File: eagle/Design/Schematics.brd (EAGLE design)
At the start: 101.6 x 55.9 mm, 66 parts, among them IC1 LM1117, IC2 CY7C68013A-56PVXC, IC3 ADS7042DCU, IC4 ADS7042DCU, Q1 SI2369DS, Q2 24MHz, X1 MPT2, X10 MPT3, X11 MPT2, X12 MPT2, X13 MPT2, X14 MPT2, X15 MPT2, X16 MPT2, X2 PN61729-S, X3 MPT2, X4 MPT2, X5 MPT2, X6 MPT2, X7 MPT2, X8 MPT2, X9 MPT3

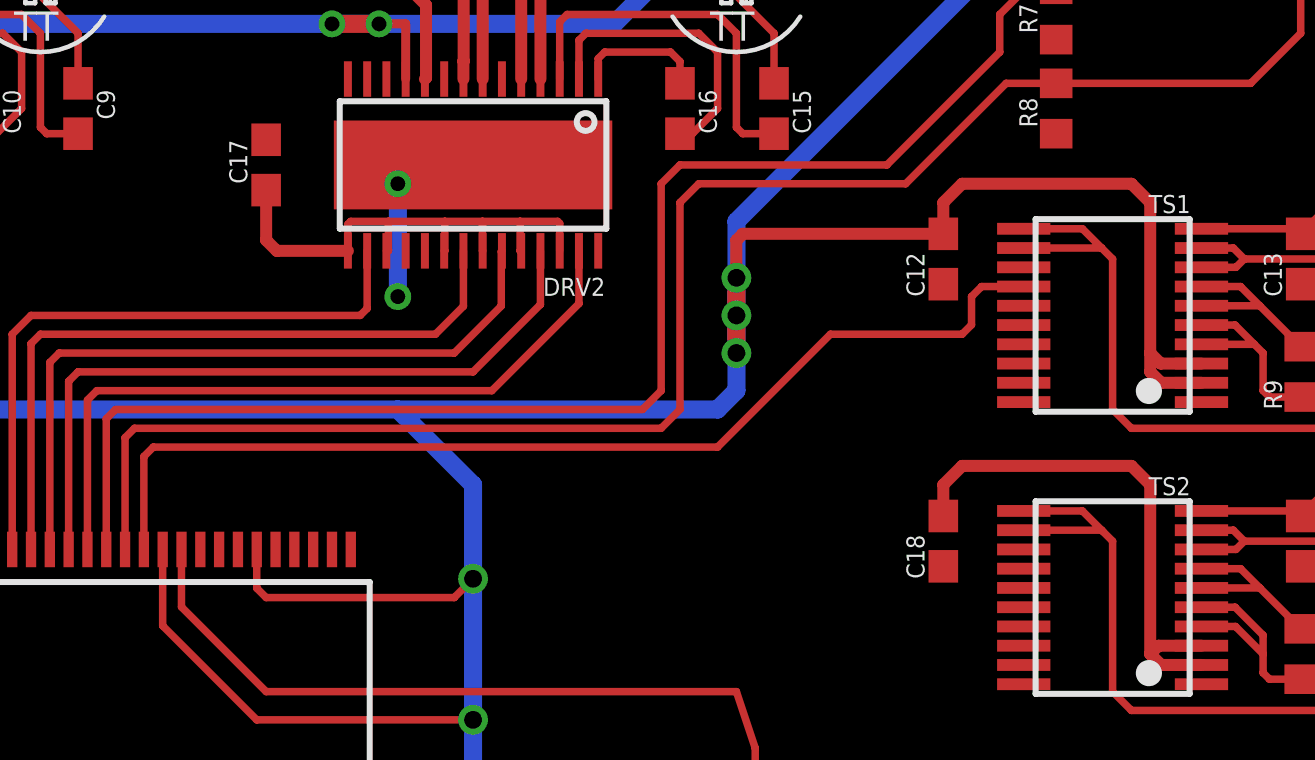
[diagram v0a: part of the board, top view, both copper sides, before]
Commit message: Routed nets for Temp Sensor #1.
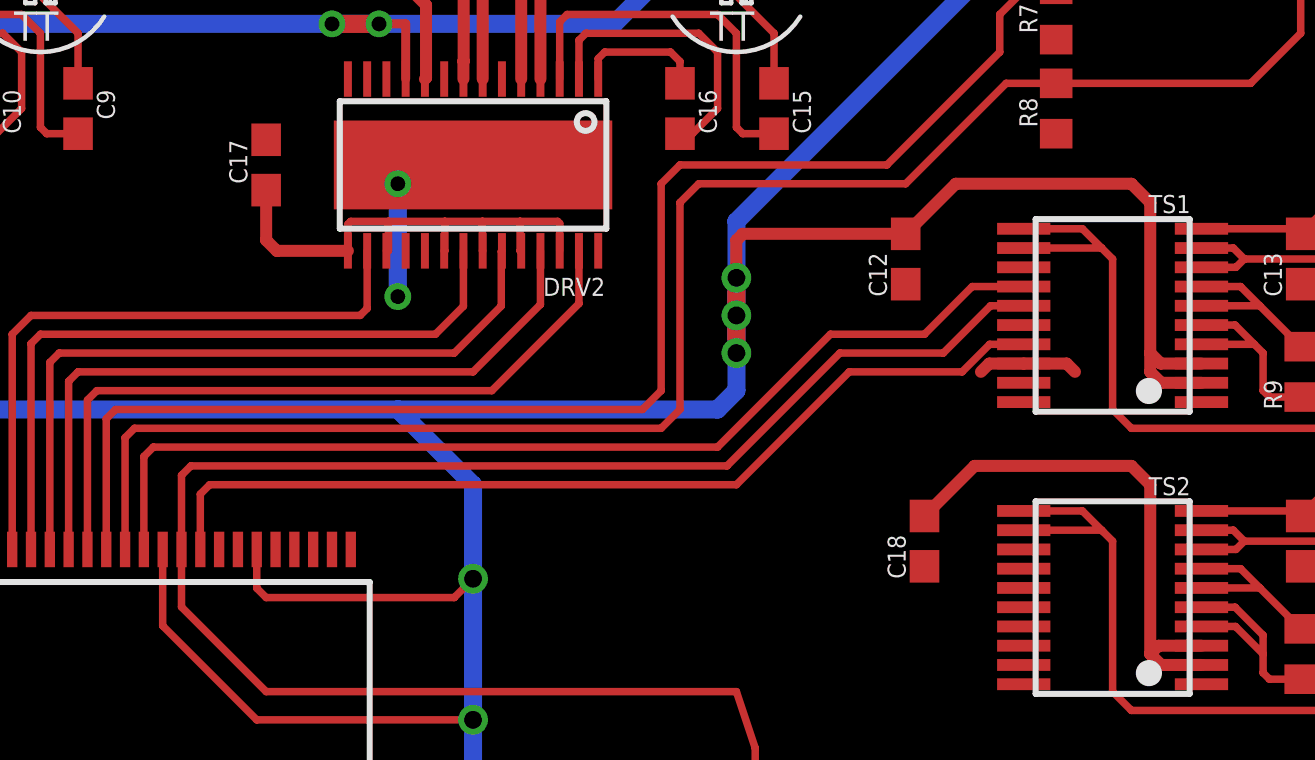
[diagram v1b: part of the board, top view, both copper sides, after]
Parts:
- moved C12 1.27 mm to (75.6, 34.9)
- moved C18 0.63 mm to (76.2, 25.4)
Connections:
- net SPI_SDO: now also IC2.37; no longer IC2.36
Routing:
- net SPI_SCLK: track 27.7 -> 61.0 mm
- net SPI_SDO: track 0.00 -> 31.8 mm
- net GND: track 8.89 -> 12.3 mm
- net +3P3V: track 358.5 -> 357.9 mm
- net SPI_SDI: track 35.8 -> 35.2 mm
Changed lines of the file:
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@@
 <attribute name="NAME" x="95.758" y="27.559" size="0.6096" layer="25" rot="R270"/>
 </element>
-<element name="C12" library="resistor" package="C0603" value="200n" x="76.835" y="34.925" smashed="yes" rot="R270">
-<attribute name="NAME" x="76.2" y="33.655" size="0.6096" layer="25" rot="R90"/>
-</element>
-<element name="C18" library="resistor" package="C0603" value="200n" x="76.835" y="25.4" smashed="yes" rot="R270">
-<attribute name="NAME" x="76.2" y="24.13" size="0.6096" layer="25" rot="R90"/>
+<element name="C12" library="resistor" package="C0603" value="200n" x="75.565" y="34.925" smashed="yes" rot="R270">
+<attribute name="NAME" x="74.93" y="33.655" size="0.6096" layer="25" rot="R90"/>
+</element>
+<element name="C18" library="resistor" package="C0603" value="200n" x="76.2" y="25.4" smashed="yes" rot="R270">
+<attribute name="NAME" x="75.565" y="24.13" size="0.6096" layer="25" rot="R90"/>
 </element>
 <element name="C13" library="resistor" package="C0603" value="100n" x="88.9" y="34.925" smashed="yes" rot="R270">
@@
 <contactref element="C12" pad="2"/>
 <contactref element="C18" pad="2"/>
-<wire x1="79.55" y1="25.12" x2="79.55" y2="21.87" width="0" layer="19" extent="1-1"/>
-<wire x1="79.55" y1="31.395" x2="79.55" y2="34.645" width="0" layer="19" extent="1-1"/>
+<wire x1="79.55" y1="31.395" x2="78.385" y2="31.395" width="0.4064" layer="1"/>
+<wire x1="78.385" y1="31.395" x2="78.105" y2="31.115" width="0.4064" layer="1"/>
+<wire x1="79.55" y1="31.395" x2="81" y2="31.395" width="0.4064" layer="1"/>
+<wire x1="81" y1="31.395" x2="81.28" y2="31.115" width="0.4064" layer="1"/>
+<wire x1="79.55" y1="21.87" x2="79.55" y2="25.12" width="0" layer="19" extent="1-1"/>
 </signal>
 <signal name="+3P3V">
@@
 <wire x1="83.82" y1="31.75" x2="83.82" y2="36.83" width="0.4064" layer="1"/>
 <wire x1="83.82" y1="36.83" x2="83.185" y2="37.465" width="0.4064" layer="1"/>
-<wire x1="83.185" y1="37.465" x2="77.47" y2="37.465" width="0.4064" layer="1"/>
-<wire x1="77.47" y1="37.465" x2="76.835" y2="36.83" width="0.4064" layer="1"/>
-<wire x1="76.835" y1="36.83" x2="76.835" y2="35.775" width="0.4064" layer="1"/>
 <wire x1="85.55" y1="30.745" x2="84.19" y2="30.745" width="0.4064" layer="1"/>
 <wire x1="84.19" y1="30.745" x2="83.82" y2="31.115" width="0.4064" layer="1"/>
 <wire x1="83.82" y1="31.115" x2="83.82" y2="31.75" width="0.4064" layer="1"/>
-<wire x1="76.835" y1="26.25" x2="76.835" y2="27.305" width="0.4064" layer="1"/>
-<wire x1="76.835" y1="27.305" x2="77.47" y2="27.94" width="0.4064" layer="1"/>
-<wire x1="77.47" y1="27.94" x2="83.185" y2="27.94" width="0.4064" layer="1"/>
 <wire x1="83.185" y1="27.94" x2="83.82" y2="27.305" width="0.4064" layer="1"/>
 <wire x1="83.82" y1="27.305" x2="83.82" y2="21.59" width="0.4064" layer="1"/>
@@
 <wire x1="85.55" y1="21.87" x2="84.1" y2="21.87" width="0.4064" layer="1"/>
 <wire x1="84.1" y1="21.87" x2="83.82" y2="21.59" width="0.4064" layer="1"/>
-<wire x1="76.835" y1="35.775" x2="70.065" y2="35.775" width="0.4064" layer="1"/>
+<wire x1="75.565" y1="35.775" x2="70.065" y2="35.775" width="0.4064" layer="1"/>
 <wire x1="70.065" y1="35.775" x2="69.85" y2="35.56" width="0.4064" layer="1"/>
 <wire x1="69.85" y1="35.56" x2="69.85" y2="34.29" width="0.4064" layer="1"/>
+<wire x1="83.185" y1="37.465" x2="77.255" y2="37.465" width="0.4064" layer="1"/>
+<wire x1="83.185" y1="27.94" x2="77.89" y2="27.94" width="0.4064" layer="1"/>
+<wire x1="77.89" y1="27.94" x2="76.2" y2="26.25" width="0.4064" layer="1"/>
+<wire x1="77.255" y1="37.465" x2="75.565" y2="35.775" width="0.4064" layer="1"/>
 <wire x1="84.19" y1="30.745" x2="83.185" y2="27.94" width="0" layer="19" extent="1-1"/>
 </signal>
@@
 <wire x1="49.8475" y1="25.12" x2="49.8475" y2="28.2575" width="0.254" layer="1"/>
 <wire x1="49.8475" y1="28.2575" x2="50.165" y2="28.575" width="0.254" layer="1"/>
-<wire x1="79.55" y1="33.995" x2="78.1275" y2="33.995" width="0.254" layer="1"/>
-<wire x1="78.1275" y1="33.995" x2="77.7875" y2="33.655" width="0.254" layer="1"/>
-<wire x1="77.7875" y1="33.655" x2="77.7875" y2="32.7025" width="0.254" layer="1"/>
-<wire x1="77.7875" y1="32.7025" x2="77.47" y2="32.385" width="0.254" layer="1"/>
-<wire x1="77.47" y1="32.385" x2="73.025" y2="32.385" width="0.254" layer="1"/>
+<wire x1="79.55" y1="33.995" x2="77.81" y2="33.995" width="0.254" layer="1"/>
 <wire x1="73.025" y1="32.385" x2="69.215" y2="28.575" width="0.254" layer="1"/>
 <wire x1="69.215" y1="28.575" x2="50.165" y2="28.575" width="0.254" layer="1"/>
-<wire x1="77.47" y1="32.385" x2="79.55" y2="24.47" width="0" layer="19" extent="1-1"/>
+<wire x1="77.81" y1="33.995" x2="76.2" y2="32.385" width="0.254" layer="1"/>
+<wire x1="76.2" y1="32.385" x2="73.025" y2="32.385" width="0.254" layer="1"/>
+<wire x1="76.2" y1="32.385" x2="79.55" y2="24.47" width="0" layer="19" extent="1-1"/>
 </signal>
 <signal name="SPI_SDO">
 <contactref element="IC3" pad="3"/>
 <contactref element="IC4" pad="3"/>
-<contactref element="IC2" pad="36"/>
 <contactref element="TS2" pad="17"/>
 <contactref element="TS1" pad="17"/>
-<wire x1="79.55" y1="22.52" x2="79.55" y2="32.045" width="0" layer="19" extent="1-1"/>
+<contactref element="IC2" pad="37"/>
+<wire x1="51.7525" y1="25.12" x2="51.7525" y2="26.9875" width="0.254" layer="1"/>
+<wire x1="51.7525" y1="26.9875" x2="52.07" y2="27.305" width="0.254" layer="1"/>
+<wire x1="52.07" y1="27.305" x2="69.85" y2="27.305" width="0.254" layer="1"/>
+<wire x1="77.47" y1="31.115" x2="73.66" y2="31.115" width="0.254" layer="1"/>
+<wire x1="79.55" y1="32.045" x2="78.4" y2="32.045" width="0.254" layer="1"/>
+<wire x1="78.4" y1="32.045" x2="77.47" y2="31.115" width="0.254" layer="1"/>
+<wire x1="73.66" y1="31.115" x2="69.85" y2="27.305" width="0.254" layer="1"/>
+<wire x1="77.47" y1="31.115" x2="79.55" y2="22.52" width="0" layer="19" extent="1-1"/>
 <wire x1="77.19" y1="11.815" x2="79.55" y2="22.52" width="0" layer="19" extent="1-1"/>
 <wire x1="77.19" y1="4.195" x2="77.19" y2="11.815" width="0" layer="19" extent="1-1"/>
-<wire x1="52.3875" y1="25.12" x2="79.55" y2="22.52" width="0" layer="19" extent="1-1"/>
 </signal>
 <signal name="N$39">
@@
 <contactref element="TS2" pad="15"/>
 <contactref element="TS1" pad="15"/>
-<wire x1="79.55" y1="23.82" x2="79.55" y2="33.345" width="0" layer="19" extent="1-1"/>
-<wire x1="69.85" y1="20.32" x2="79.55" y2="23.82" width="0" layer="19" extent="1-1"/>
+<wire x1="51.1175" y1="25.12" x2="51.1175" y2="27.6225" width="0.254" layer="1"/>
+<wire x1="51.1175" y1="27.6225" x2="51.435" y2="27.94" width="0.254" layer="1"/>
+<wire x1="51.435" y1="27.94" x2="69.5325" y2="27.94" width="0.254" layer="1"/>
+<wire x1="79.55" y1="33.345" x2="78.43" y2="33.345" width="0.254" layer="1"/>
+<wire x1="78.43" y1="33.345" x2="76.835" y2="31.75" width="0.254" layer="1"/>
+<wire x1="76.835" y1="31.75" x2="73.3425" y2="31.75" width="0.254" layer="1"/>
+<wire x1="73.3425" y1="31.75" x2="69.5325" y2="27.94" width="0.254" layer="1"/>
+<wire x1="76.835" y1="31.75" x2="79.55" y2="23.82" width="0" layer="19" extent="1-1"/>
 <wire x1="70.485" y1="10.16" x2="70.485" y2="14.605" width="0" layer="19" extent="1-1"/>
 <wire x1="77.19" y1="12.315" x2="70.485" y2="10.16" width="0" layer="19" extent="1-1"/>

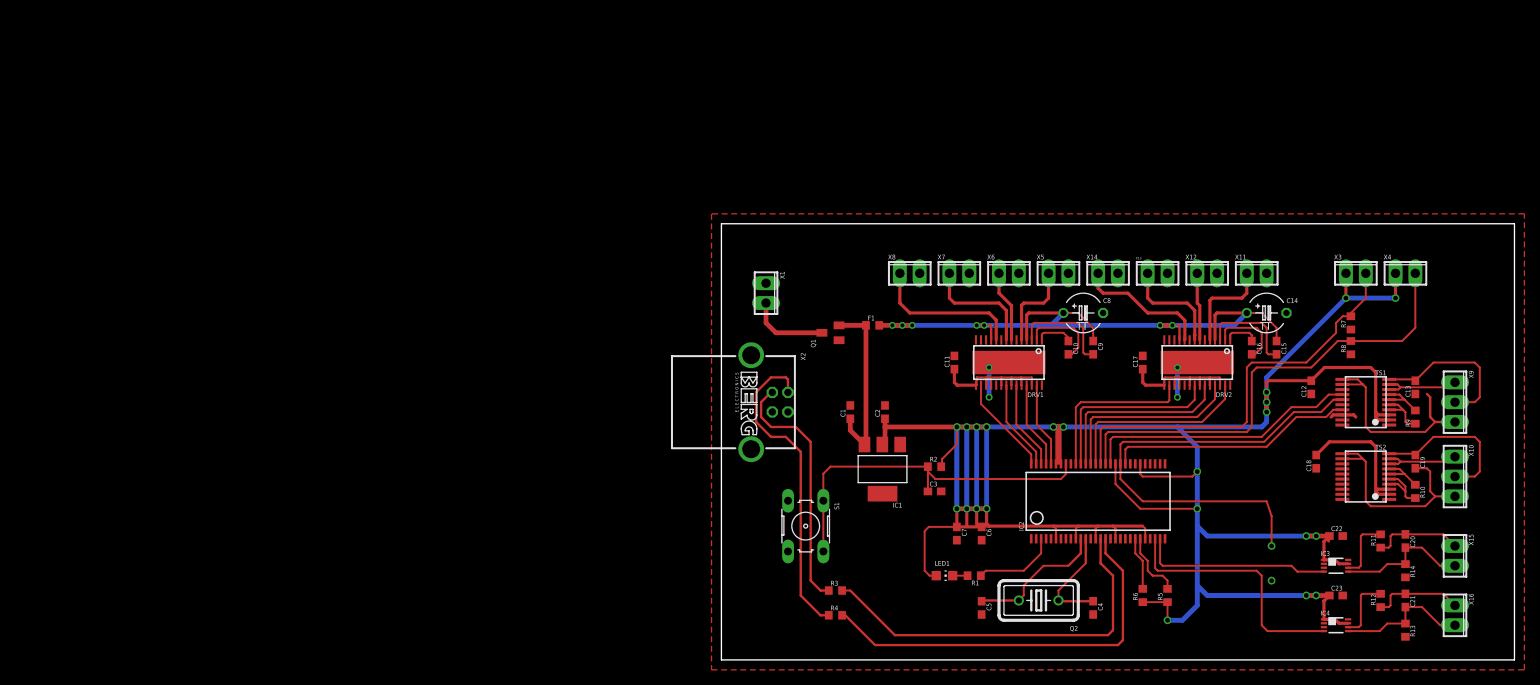
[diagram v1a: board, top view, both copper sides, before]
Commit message: Goodbye USB, hello Pi
Completely changed the direction of the hardware development.
Originally wanted to utilize a USB interface to plug into any PC but
found it was easier (and cheaper) to by a Raspberry Pi for $35 and build
an expansion board to control the brew hardware.  Created a barebone set
of schematics and layout.
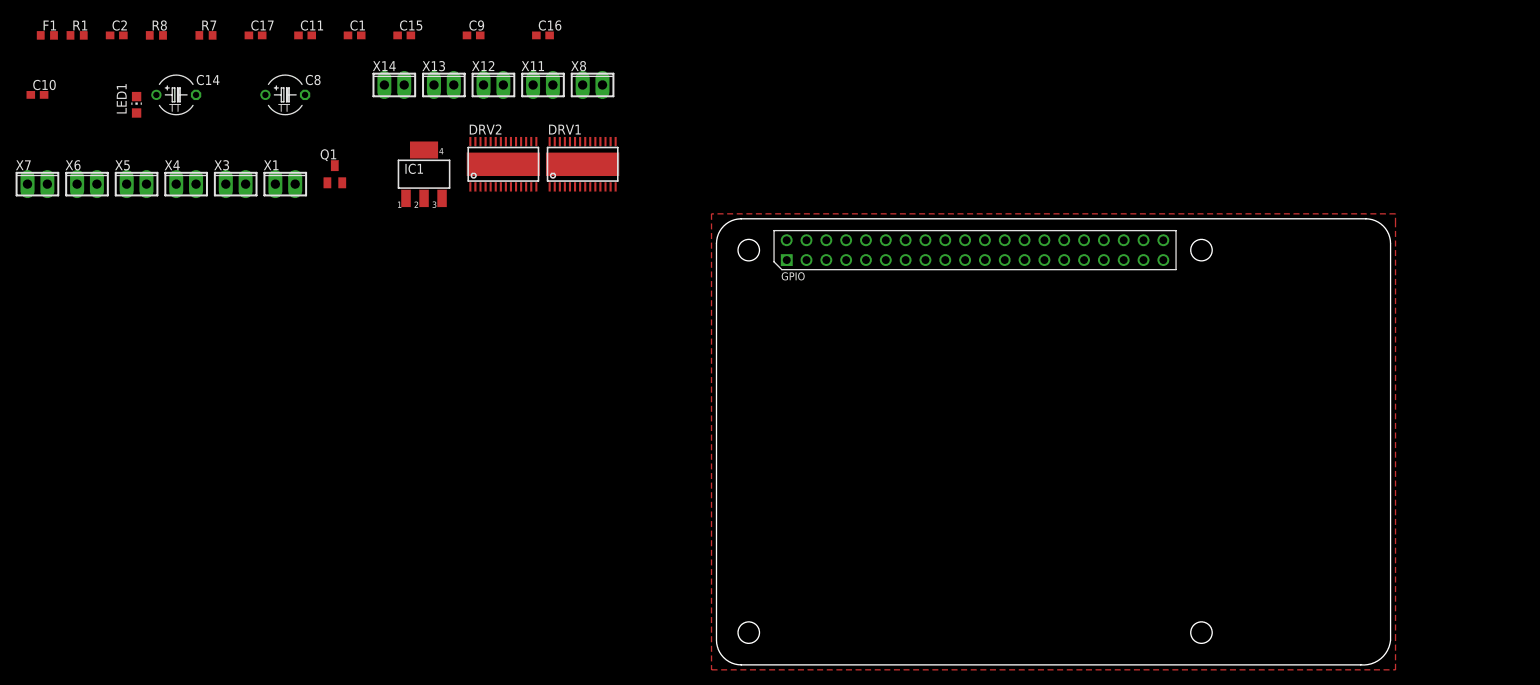
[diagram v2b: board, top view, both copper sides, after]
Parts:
- removed C12, C18: 200n, resistor:C0603
- removed C13, C19, C20, C21: 100n, resistor:C0603
- removed C22, C23: 1u, resistor:C0603
- removed C3, C7: .1u, resistor:C0603
- removed C4, C5: 27p, resistor:C0603
- removed C6: 2.2u, resistor:C0603
- removed IC2: CY7C68013A-56PVXC, cypress:SSOP56
- removed IC3, IC4: ADS7042DCU, texas:DCU_(R-PDSO-G8)
- removed Q2: 24MHz, crystal:HC18U-V
- removed R10, R9: 390 .1%, resistor:R0603
- removed R11, R12, R2: 100K, resistor:R0603
- removed R13, R14: DNS, resistor:R0603
- removed R3, R4: 22, resistor:R0603
- removed R5, R6: 2.2K, resistor:R0603
- removed S1: (no value), switch-omron:B3F-10XX
- removed TS1, TS2: MAX31865, Common:SSOP20
- removed X10, X9: MPT3, Common:3POL254
- removed X15, X16: MPT2, Common:2POL254
- removed X2: PN61729-S, con-berg:PN61729-S
- added PCB: RPI3, Custom:RPI3
- C1: value 10u -> 0.22u
- C2: value 100u -> 0.1u
- IC1: value LM1117 -> LM340S; device Common:SOT223 -> linear:SOT223
- moved R8 158.2 mm to (-72.4, 80.0), turned to 0 degrees
- moved X4 156.6 mm to (-68.6, 61.0)
- moved R7 151.2 mm to (-66.0, 80.0), turned to 0 degrees
- moved X3 144.0 mm to (-62.2, 61.0)
- moved C14 142.5 mm to (-69.8, 72.4)
- moved C10 136.0 mm to (-87.6, 72.4), turned to 0 degrees
- moved R1 134.2 mm to (-82.5, 80.0), turned to 0 degrees
- moved C17 121.1 mm to (-59.7, 80.0), turned to 0 degrees
- moved LED1 119.8 mm to (-74.9, 71.1), turned to 0 degrees
- moved C15 118.7 mm to (-40.6, 80.0), turned to 0 degrees
- moved X5 118.7 mm to (-74.9, 61.0)
- moved X6 118.7 mm to (-81.3, 61.0)
- moved X7 118.7 mm to (-87.6, 61.0)
- moved F1 112.1 mm to (-86.4, 80.0)
- moved C2 109.6 mm to (-77.5, 80.0), turned to 0 degrees
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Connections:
- removed net !ADC1_CS: IC2.27, IC3.4
- removed net !ADC2_CS: IC2.26, IC4.4
- removed net !TS1_CS: TS1.16
- removed net !TS2_CS: TS2.16
- removed net +5V_USB: X2.4
- removed net DMINUS: IC2.16, R4.2
- removed net DPLUS: IC2.15, R3.2
- removed net N$1: IC2.22, R6.2
- removed net N$11: R10.1, TS2.6, TS2.7
- removed net N$12: IC2.5
- removed net N$14: IC3.6, R11.2
- removed net N$15: R10.2, TS2.4, TS2.5
- removed net N$16: C20.1, R11.1, X15.1
- removed net N$17: TS2.8, TS2.9, X10.1
- removed net N$18: C19.2, TS2.11, TS2.12, X10.3
- removed net N$19: C19.1, TS2.10, X10.2
- removed net N$2: IC2.23, R5.2
- removed net N$20: TS1.1
- removed net N$21: TS2.1
- removed net N$3: R4.1, X2.2
- removed net N$36: IC2.8
- removed net N$37: IC2.9
- removed net N$38: IC2.20
- removed net N$4: R3.1, X2.3
- removed net N$40: IC4.6, R12.2
- removed net N$45: C13.2, TS1.11, TS1.12, X9.3
- removed net N$46: C21.1, R12.1, X16.1
- removed net N$48: C20.2, IC3.5, R14.1, X15.2
- removed net N$49: C21.2, IC4.5, R13.1, X16.2
- removed net N$5: R9.1, TS1.6, TS1.7
- removed net N$50: IC2.25
- removed net N$54: IC2.1
- removed net N$55: IC2.2
- removed net N$6: R9.2, TS1.4, TS1.5
- removed net N$7: TS1.8, TS1.9, X9.1
- removed net N$9: C13.1, TS1.10, X9.2
- removed net RESETN: C3.1, IC2.49, R2.1, S1.1, S1.2
- removed net SPI_SCLK: IC2.38, IC3.2, IC4.2, TS1.15, TS2.15
- removed net SPI_SDI: IC2.40, TS1.14, TS2.14
- removed net SPI_SDO: IC2.37, IC3.3, IC4.3, TS1.17, TS2.17
- removed net XTALIN: C4.1, IC2.12, Q2.1
- removed net XTALOUT: C5.1, IC2.11, Q2.2
- new net +5V: C2.1, IC1.3, PCB.2, PCB.4
- net !DRV1_RESET: no longer IC2.56
- net !DRV2_RESET: no longer IC2.47
- net +3P3V: now also PCB.1, PCB.17; no longer C12.1, C18.1, C2.1, C22.1, C23.1, C6.1, C7.1, IC1.2, IC2.10, IC2.14, IC2.18, IC2.24, IC2.34, IC2.39, IC2.50, IC2.51, IC2.6, IC3.1, IC3.7, IC4.1, IC4.7, R2.2, R5.1, R6.1, TS1.2, TS1.3, TS2.2, TS2.3
- net DRV1_IN1: no longer IC2.52
- net DRV1_IN2: no longer IC2.53
- net DRV1_IN3: no longer IC2.54
- net DRV1_IN4: no longer IC2.55
- net DRV2_IN1: no longer IC2.43
- net DRV2_IN2: no longer IC2.44
- net DRV2_IN3: no longer IC2.45
- net DRV2_IN4: no longer IC2.46
- net GND: now also IC1.2, IC1.4, PCB.14, PCB.20, PCB.25, PCB.30, PCB.34, PCB.39, PCB.6, PCB.9; no longer C12.2, C18.2, C22.2, C23.2, C3.2, C4.2, C5.2, C6.2, C7.2, IC1.1, IC2.13, IC2.17, IC2.19, IC2.21, IC2.33, IC2.35, IC2.4, IC2.48, IC2.7, IC3.8, IC4.8, R13.2, R14.2, S1.3, S1.4, TS1.13, TS1.18, TS1.19, TS2.13, TS2.18, TS2.19, X2.1, X2.S1, X2.S2
- net N$13: now also IC1.1; no longer IC1.3
- net STATUS: no longer IC2.3
- net SW1: no longer IC2.42
- net SW2: no longer IC2.41
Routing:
- net +3P3V: track 357.9 -> 0.00 mm, vias 22 -> 0
- net +12V: track 88.6 -> 0.00 mm, vias 7 -> 0
- net SPI_SCLK: track 61.0 -> 0.00 mm, vias 2 -> 0
- net SW2: track 60.2 -> 0.00 mm
- net SW1: track 53.6 -> 0.00 mm
- net DMINUS: track 51.7 -> 0.00 mm
- net DPLUS: track 49.7 -> 0.00 mm
- net RESETN: track 46.6 -> 0.00 mm
- net N$3: track 40.8 -> 0.00 mm
- net SPI_SDI: track 35.2 -> 0.00 mm
- net !ADC2_CS: track 32.5 -> 0.00 mm
- net N$4: track 32.2 -> 0.00 mm
- net SPI_SDO: track 31.8 -> 0.00 mm
- net N$18: track 28.9 -> 0.00 mm
- net N$45: track 27.4 -> 0.00 mm
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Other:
- board size 101.6 x 55.9 mm -> 86.4 x 57.2 mm
